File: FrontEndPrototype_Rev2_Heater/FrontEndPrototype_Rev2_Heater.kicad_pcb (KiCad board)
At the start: 4 copper layers, 63.5 x 63.5 mm, 16 parts, among them J1 Conn_01x02_Pin, J2 Conn_01x02_Pin, J3 Conn_01x02_Pin, J4 Conn_01x02_Pin

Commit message: Boards nearly finalized
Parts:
- removed REF** (x8): PogoClearanceHole, GenIILibrary:PogoClearanceHole
- added H1: PogoPinClearanceHole, GenIILibrary:PogoClearanceHole, F.Cu at (89.0, 26.8)
- added H10: PogoPinClearanceHole, GenIILibrary:PogoClearanceHole, F.Cu at (93.4, -9.65)
- added H11: PogoPinClearanceHole, GenIILibrary:PogoClearanceHole, F.Cu at (86.9, -12.7)
- added H12: PogoPinClearanceHole, GenIILibrary:PogoClearanceHole, F.Cu at (86.9, -10.1)
- added H13: PogoPinClearanceHole, GenIILibrary:PogoClearanceHole, F.Cu at (96.0, -12.3)
- added H14: PogoPinClearanceHole, GenIILibrary:PogoClearanceHole, F.Cu at (96.0, -9.65)
- added H15: PogoPinClearanceHole, GenIILibrary:PogoClearanceHole, F.Cu at (89.5, -12.7)
- added H16: PogoPinClearanceHole, GenIILibrary:PogoClearanceHole, F.Cu at (89.5, -10.1)
- added H2: PogoPinClearanceHole, GenIILibrary:PogoClearanceHole, F.Cu at (89.2, 36.6)
- added H3: PogoPinClearanceHole, GenIILibrary:PogoClearanceHole, F.Cu at (93.4, 21.8)
- added H4: PogoPinClearanceHole, GenIILibrary:PogoClearanceHole, F.Cu at (94.3, 40.9)
- added H5: PogoPinClearanceHole, GenIILibrary:PogoClearanceHole, F.Cu at (103.8, 22.3)
- added H6: PogoPinClearanceHole, GenIILibrary:PogoClearanceHole, F.Cu at (107.8, 36.0)
- added H7: PogoPinClearanceHole, GenIILibrary:PogoClearanceHole, F.Cu at (108.2, 26.8)
- added H8: PogoPinClearanceHole, GenIILibrary:PogoClearanceHole, F.Cu at (103.4, 41.1)
- added H9: PogoPinClearanceHole, GenIILibrary:PogoClearanceHole, F.Cu at (93.4, -12.3)
- added J5: Conn_01x02_Pin, GenIILibrary:Samtec_Pin_Socket_SS_102_G_2, F.Cu at (118.5, 31.7)
- added J6: Conn_01x02_Pin, GenIILibrary:Samtec_Pin_Socket_SS_102_G_2, F.Cu at (98.6, 51.0)
- added J7: Conn_01x02_Pin, GenIILibrary:Samtec_Pin_Socket_SS_102_G_2, F.Cu at (78.5, 31.7)
- added J8: Conn_01x02_Pin, GenIILibrary:Samtec_Pin_Socket_SS_102_G_2, F.Cu at (98.6, 11.1)
- added R10: 50, Resistor_SMD:R_2010_5025Metric_Pad1.40x2.65mm_HandSolder, B.Cu at (98.6, 24.2)
- added R11: 50, Resistor_SMD:R_2010_5025Metric_Pad1.40x2.65mm_HandSolder, B.Cu at (87.8, 21.0)
- added R12: 50, Resistor_SMD:R_2010_5025Metric_Pad1.40x2.65mm_HandSolder, B.Cu at (91.1, 31.7)
- added R13: 50, Resistor_SMD:R_2010_5025Metric_Pad1.40x2.65mm_HandSolder, B.Cu at (106.1, 31.7)
- added R14: 50, Resistor_SMD:R_2010_5025Metric_Pad1.40x2.65mm_HandSolder, B.Cu at (98.6, 39.2)
- added R15: 50, Resistor_SMD:R_2010_5025Metric_Pad1.40x2.65mm_HandSolder, B.Cu at (87.8, 42.5)
- added R16: 50, Resistor_SMD:R_2010_5025Metric_Pad1.40x2.65mm_HandSolder, B.Cu at (109.3, 42.5)
- added R9: 50, Resistor_SMD:R_2010_5025Metric_Pad1.40x2.65mm_HandSolder, B.Cu at (109.3, 21.0)
- added TH5: Thermistor_NTC, Resistor_SMD:R_0603_1608Metric_Pad0.98x0.95mm_HandSolder, F.Cu at (114.8, 31.7)
- added TH6: Thermistor_NTC, Resistor_SMD:R_0603_1608Metric_Pad0.98x0.95mm_HandSolder, F.Cu at (98.6, 15.5)
- added TH7: Thermistor_NTC, Resistor_SMD:R_0603_1608Metric_Pad0.98x0.95mm_HandSolder, F.Cu at (82.3, 31.7)
- added TH8: Thermistor_NTC, Resistor_SMD:R_0603_1608Metric_Pad0.98x0.95mm_HandSolder, F.Cu at (98.6, 48.0)
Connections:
- net GND renamed GND_1
- net Vdd_Heater renamed Vdd_Heater_1
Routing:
- net HGND: track 0.00 -> 10.8 mm, vias 0 -> 8
- net Vdd_Heater_2: track 0.00 -> 10.8 mm, vias 0 -> 8
- added copper zone on F.Cu, net GND_2
- added copper zone on In1.Cu, net HGND
- added copper zone on In2.Cu, net HGND
- added copper zone on B.Cu, net Vdd_Heater_2
- added copper zone on F.Cu, net Vdd_Heater_2
- removed copper zone on F.Cu, net GND_1
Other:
- board size 63.5 x 63.5 mm -> 130.3 x 63.5 mm
- board text added: "Type I"
- board text added: "Type II"

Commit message: Nearly Finalized Boards
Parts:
- removed H1, H2, H3, H4, H5, H6, H7, H8: PogoPinClearanceHole, GenIILibrary:PogoClearanceHole
- removed J2, J3, J4, J8: Conn_01x02_Pin, GenIILibrary:Samtec_Pin_Socket_SS_102_G_2
- removed TH1, TH2, TH3, TH4, TH6, TH8: Thermistor_NTC, Resistor_SMD:R_0603_1608Metric_Pad0.98x0.95mm_HandSolder
- moved J1 96.1 mm to (98.6, 15.0), turned to -90 degrees
- moved H12 53.1 mm to (102.5, 40.7)
- moved H10 51.6 mm to (93.1, 41.9)
- moved H14 48.7 mm to (108.7, 37.4)
- moved H9 48.0 mm to (89.7, 35.6)
- moved H16 41.9 mm to (107.5, 27.7)
- moved J7 40.8 mm to (119.3, 31.7), turned to 0 degrees
- moved H15 39.0 mm to (88.4, 26.2)
- moved H11 38.3 mm to (104.1, 21.4)
- moved H13 35.1 mm to (94.6, 22.7)
- moved J6 28.3 mm to (77.8, 31.7), turned to 0 degrees
- moved J5 26.0 mm to (98.6, 48.5), turned to 90 degrees
- turned TH5 to -90 degrees
- turned TH7 to -90 degrees
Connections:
- J1 pad 1: Vdd_Heater_1 -> Vdd_Heater_2
- J1 pad 2: GND_1 -> Net-(J1-Pin_2)
- J5 pad 2: GND_2 -> Net-(J1-Pin_2)
- J6 pad 1: HGND -> Net-(J6-Pin_1)
- J6 pad 2: GND_2 -> Net-(J6-Pin_2)
- R10 pad 1: HGND -> Net-(J1-Pin_2)
- R11 pad 1: HGND -> Net-(J1-Pin_2)
- R12 pad 1: HGND -> Net-(J1-Pin_2)
- R13 pad 1: HGND -> Net-(J1-Pin_2)
- R14 pad 1: HGND -> Net-(J1-Pin_2)
- R15 pad 1: HGND -> Net-(J1-Pin_2)
- R16 pad 1: HGND -> Net-(J1-Pin_2)
- R9 pad 1: HGND -> Net-(J1-Pin_2)
- TH5 pad 1: Vdd_Heater_2 -> Net-(J7-Pin_1)
- TH5 pad 2: Net-(J7-Pin_1) -> Net-(J7-Pin_2)
- TH7 pad 1: Vdd_Heater_2 -> Net-(J6-Pin_1)
- TH7 pad 2: Net-(J8-Pin_1) -> Net-(J6-Pin_2)
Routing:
- net Vdd_Heater_1: track 2428.9 -> 0.00 mm, vias 6 -> 0
- net Net-(J2-Pin_1): track 62.8 -> 0.00 mm, vias 3 -> 0
- net Net-(J4-Pin_1): track 53.1 -> 0.00 mm, vias 2 -> 0
- net Net-(J4-Pin_2): track 21.7 -> 0.00 mm, vias 1 -> 0
- net Net-(J2-Pin_2): track 20.2 -> 0.00 mm, vias 1 -> 0
- net Net-(J1-Pin_2): track 0.00 -> 18.9 mm, vias 0 -> 8
- net HGND: track 10.8 -> 0.00 mm, vias 8 -> 0
- net Vdd_Heater_2: track 10.8 -> 18.9 mm, vias 8 -> 17
- net Net-(J7-Pin_2): track 0.00 -> 4.65 mm
- net Net-(J7-Pin_1): track 0.00 -> 4.65 mm
- net Net-(J6-Pin_2): track 0.00 -> 4.65 mm
- net Net-(J6-Pin_1): track 0.00 -> 4.65 mm
- net GND_1: track 4.28 -> 0.00 mm
- added copper zone on In1.Cu, net Net-(J1-Pin_2)
- added copper zone on In2.Cu, net Net-(J1-Pin_2)
- removed copper zone on F.Cu, net GND_2
- removed copper zone on In1.Cu, net HGND
- removed copper zone on In2.Cu, net HGND
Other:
- board outline removed
- board text removed: "Type I"
- board text removed: "Type II"

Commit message: Final commit before order
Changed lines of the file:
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@@
 		)
+	)
+	(gr_rect
+		(start 74.575 11.9625)
+		(end 122.575 51.7375)
+		(stroke
+			(width 0.15)
+			(type default)
+		)
+		(fill none)
+		(layer "F.SilkS")
 	)
 	(gr_line

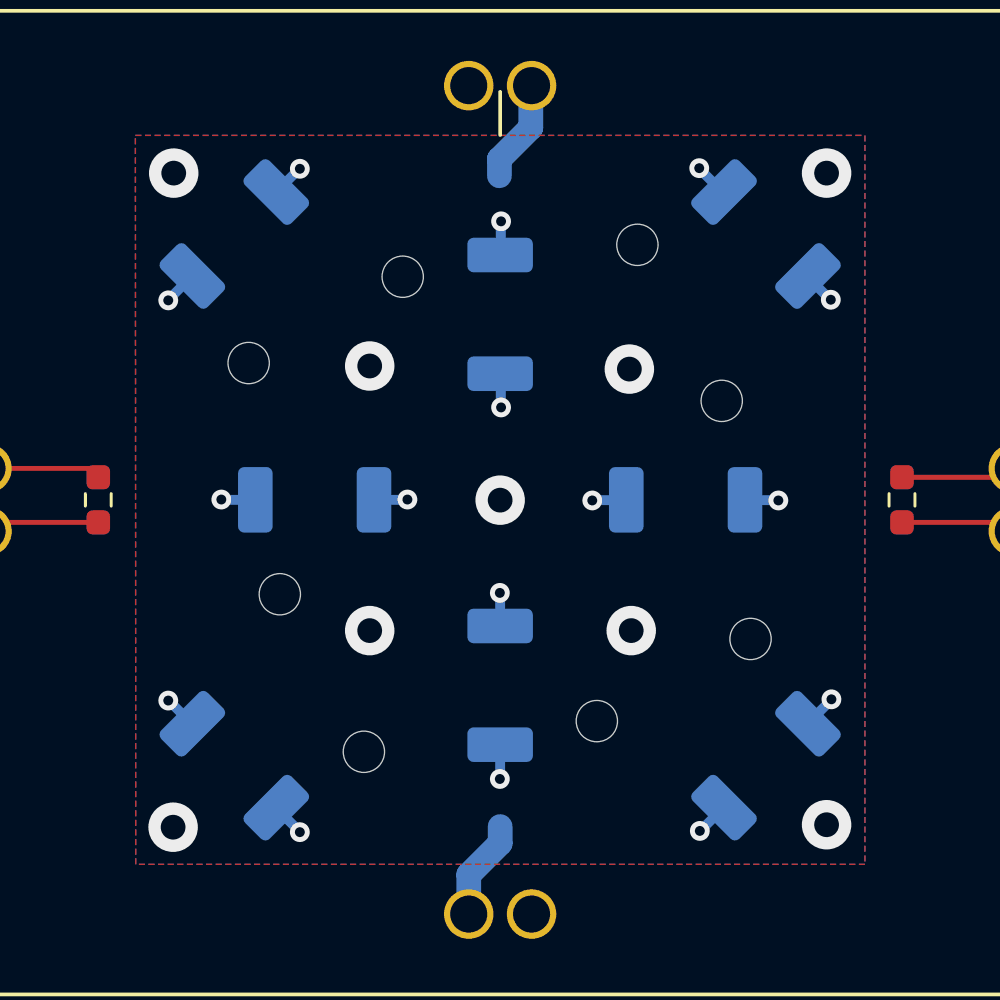
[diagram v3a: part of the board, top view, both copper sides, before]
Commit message: Updated Measurement Board with new 3V Reference
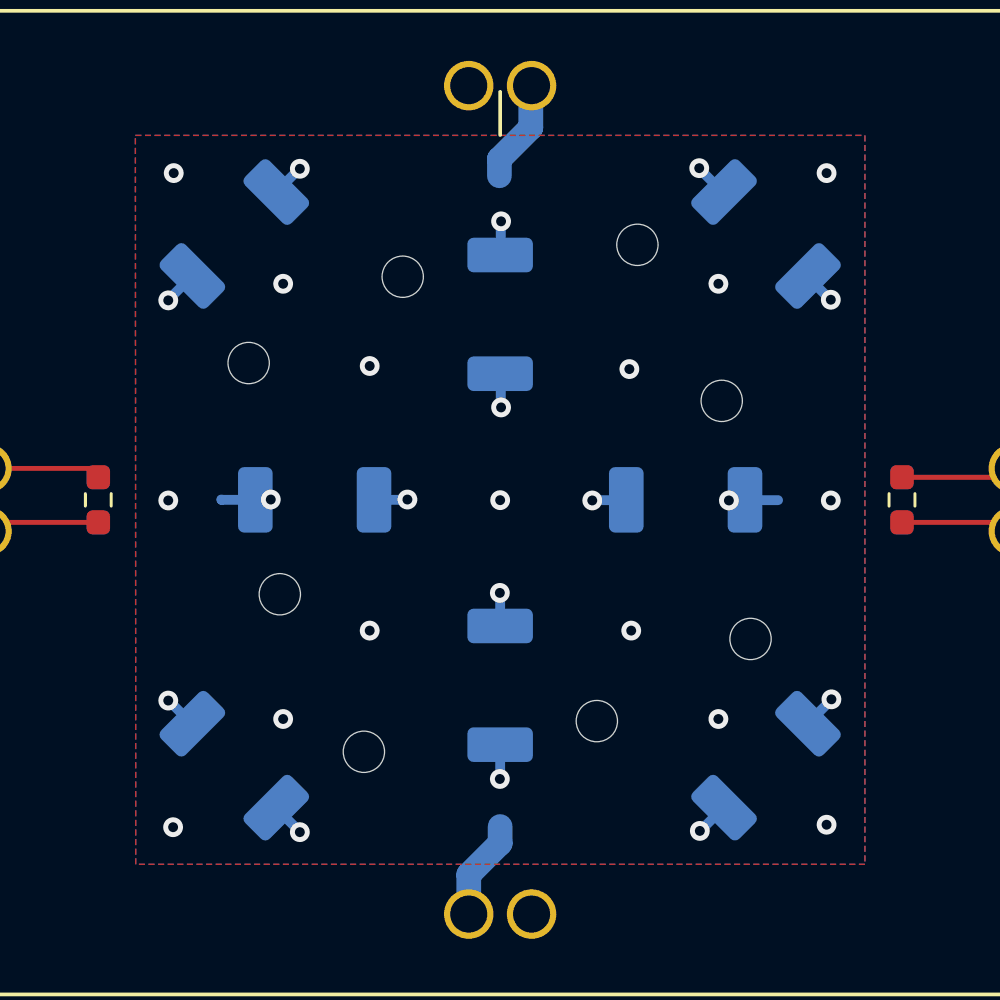
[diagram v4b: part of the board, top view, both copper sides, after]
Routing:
- net Vdd_Heater_2: vias 17 -> 19
- net Net-(J1-Pin_2): vias 8 -> 12
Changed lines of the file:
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@@
 	)
 	(via
-		(at 87.3 31.725)
+		(at 107.4 40.6)
+		(size 0.8)
+		(drill 0.4)
+		(layers "F.Cu" "B.Cu")
+		(free yes)
+		(net 1)
+	)
+	(via
+		(at 107.4 23)
+		(size 0.8)
+		(drill 0.4)
+		(layers "F.Cu" "B.Cu")
+		(free yes)
+		(net 1)
+	)
+	(via
+		(at 89.3 31.725)
 		(size 0.8)
 		(drill 0.4)
@@
 	)
 	(via
-		(at 109.825 31.7625)
+		(at 107.825 31.7625)
 		(size 0.8)
 		(drill 0.4)
@@
 		(drill 0.4)
 		(layers "F.Cu" "B.Cu")
+		(net 1)
+	)
+	(via
+		(at 89.8 23)
+		(size 0.8)
+		(drill 0.4)
+		(layers "F.Cu" "B.Cu")
+		(free yes)
+		(net 1)
+	)
+	(via
+		(at 89.8 40.6)
+		(size 0.8)
+		(drill 0.4)
+		(layers "F.Cu" "B.Cu")
+		(free yes)
 		(net 1)
 	)
@@
 	(via
 		(at 93.3 26.325)
-		(size 2)
-		(drill 1)
+		(size 0.8)
+		(drill 0.4)
 		(layers "F.Cu" "B.Cu")
 		(free yes)
@@
 	(via
 		(at 85.375 18.525)
-		(size 2)
-		(drill 1)
+		(size 0.8)
+		(drill 0.4)
 		(layers "F.Cu" "B.Cu")
 		(free yes)
@@
 	(via
 		(at 103.875 37.025)
-		(size 2)
-		(drill 1)
+		(size 0.8)
+		(drill 0.4)
 		(layers "F.Cu" "B.Cu")
 		(free yes)
@@
 	(via
 		(at 85.35 44.975)
-		(size 2)
-		(drill 1)
+		(size 0.8)
+		(drill 0.4)
 		(layers "F.Cu" "B.Cu")
 		(free yes)
@@
 	(via
 		(at 93.3 37.025)
-		(size 2)
-		(drill 1)
+		(size 0.8)
+		(drill 0.4)
 		(layers "F.Cu" "B.Cu")
 		(free yes)
@@
 	(via
 		(at 111.775 18.525)
-		(size 2)
-		(drill 1)
+		(size 0.8)
+		(drill 0.4)
 		(layers "F.Cu" "B.Cu")
 		(free yes)
@@
 	)
 	(via
+		(at 111.945979 31.7625)
+		(size 0.8)
+		(drill 0.4)
+		(layers "F.Cu" "B.Cu")
+		(free yes)
+		(net 6)
+	)
+	(via
 		(at 98.575 31.75)
-		(size 2)
-		(drill 1)
+		(size 0.8)
+		(drill 0.4)
 		(layers "F.Cu" "B.Cu")
 		(free yes)
@@
 	)
 	(via
+		(at 85.154021 31.7625)
+		(size 0.8)
+		(drill 0.4)
+		(layers "F.Cu" "B.Cu")
+		(free yes)
+		(net 6)
+	)
+	(via
 		(at 98.6125 28)
 		(size 0.8)
@@
 	(via
 		(at 111.775 44.875)
-		(size 2)
-		(drill 1)
+		(size 0.8)
+		(drill 0.4)
 		(layers "F.Cu" "B.Cu")
 		(free yes)
@@
 	(via
 		(at 103.8 26.45)
-		(size 2)
-		(drill 1)
-		(layers "F.Cu" "B.Cu")
-		(free yes)
+		(size 0.8)
+		(drill 0.4)
+		(layers "F.Cu" "B.Cu")
+		(free yes)

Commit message: Final Edit Before Check and Combine
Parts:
- added J2: Conn_01x02_Pin, GenIILibrary:Thermistor_ExtensionPad, F.Cu at (121.6, 31.7)
- added J3: Conn_01x02_Pin, GenIILibrary:Thermistor_ExtensionPad, F.Cu at (75.6, 31.7)
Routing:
- net Net-(J2-Pin_1): track 4.65 -> 7.17 mm
- net Net-(J2-Pin_2): track 4.65 -> 7.16 mm
- net Net-(J3-Pin_1): track 4.65 -> 6.97 mm
- net Net-(J3-Pin_2): track 4.65 -> 6.96 mm
- net Vdd_Heater_2: vias 19 -> 21

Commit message: Final Rev3 Commit Post Submission
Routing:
- net Vdd_Heater_2: vias 21 -> 28
- net Net-(J1-Pin_2): vias 12 -> 13
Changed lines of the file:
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@@
 			(at 0 2.279999 0)
 			(layer "B.SilkS")
+			(hide yes)
 			(effects
 				(font
@@
 			(at 0 2.279999 90)
 			(layer "B.SilkS")
+			(hide yes)
 			(effects
 				(font
@@
 			(at 0 2.279999 0)
 			(layer "B.SilkS")
+			(hide yes)
 			(effects
 				(font
@@
 			(at 0 2.279999 135)
 			(layer "B.SilkS")
+			(hide yes)
 			(effects
 				(font
@@
 			(at 0 2.279999 45)
 			(layer "B.SilkS")
+			(hide yes)
 			(effects
 				(font
@@
 			(at 0 2.279999 -135)
 			(layer "B.SilkS")
+			(hide yes)
 			(effects
 				(font
@@
 			(at 0 2.279999 -45)
 			(layer "B.SilkS")
+			(hide yes)
 			(effects
 				(font
@@
 			(at 0 2.279999 90)
 			(layer "B.SilkS")
+			(hide yes)
 			(effects
 				(font
@@
 	)
 	(via
-		(at 89.3 31.725)
+		(at 87.3125 31.7375)
 		(size 0.8)
 		(drill 0.4)
@@
 	)
 	(via
-		(at 107.825 31.7625)
+		(at 109.812501 31.75)
 		(size 0.8)
 		(drill 0.4)
@@
 		(drill 0.4)
 		(layers "F.Cu" "B.Cu")
+		(net 1)
+	)
+	(via
+		(at 98.575 31.75)
+		(size 0.8)
+		(drill 0.4)
+		(layers "F.Cu" "B.Cu")
+		(free yes)
 		(net 1)
 	)
@@
 	)
 	(via
+		(at 111.945979 35.79)
+		(size 0.8)
+		(drill 0.4)
+		(layers "F.Cu" "B.Cu")
+		(free yes)
+		(net 5)
+	)
+	(via
 		(at 85.375 18.525)
 		(size 0.8)
@@
 	)
 	(via
+		(at 94.5 45.175)
+		(size 0.8)
+		(drill 0.4)
+		(layers "F.Cu" "B.Cu")
+		(free yes)
+		(net 5)
+	)
+	(via
 		(at 106.625 18.325)
 		(size 0.8)
@@
 	)
 	(via
+		(at 102.6 45.175)
+		(size 0.8)
+		(drill 0.4)
+		(layers "F.Cu" "B.Cu")
+		(free yes)
+		(net 5)
+	)
+	(via
 		(at 111.775 18.525)
 		(size 0.8)
@@
 	)
 	(via
-		(at 98.575 31.75)
+		(at 102.3 31.7625)
+		(size 0.8)
+		(drill 0.4)
+		(layers "F.Cu" "B.Cu")
+		(net 5)
+	)
+	(via
+		(at 85.154021 31.725)
 		(size 0.8)
 		(drill 0.4)
@@
 	)
 	(via
-		(at 102.3 31.7625)
-		(size 0.8)
-		(drill 0.4)
-		(layers "F.Cu" "B.Cu")
-		(net 5)
-	)
-	(via
-		(at 85.154021 31.7625)
+		(at 98.575 28)
+		(size 0.8)
+		(drill 0.4)
+		(layers "F.Cu" "B.Cu")
+		(net 5)
+	)
+	(via
+		(at 94.5 18.35)
 		(size 0.8)
 		(drill 0.4)
@@
 	)
 	(via
-		(at 98.575 28)
-		(size 0.8)
-		(drill 0.4)
-		(layers "F.Cu" "B.Cu")
+		(at 85.154021 35.79)
+		(size 0.8)
+		(drill 0.4)
+		(layers "F.Cu" "B.Cu")
+		(free yes)
+		(net 5)
+	)
+	(via
+		(at 85.154021 27.7)
+		(size 0.8)
+		(drill 0.4)
+		(layers "F.Cu" "B.Cu")
+		(free yes)
+		(net 5)
+	)
+	(via
+		(at 102.6 18.35)
+		(size 0.8)
+		(drill 0.4)
+		(layers "F.Cu" "B.Cu")
+		(free yes)
 		(net 5)
 	)
@@
 		(size 0.8)
 		(drill 0.4)
+		(layers "F.Cu" "B.Cu")
+		(free yes)
+		(net 5)
+	)
+	(via
+		(at 111.945979 27.7)
+		(size 0.8)
+		(drill 0.4)
